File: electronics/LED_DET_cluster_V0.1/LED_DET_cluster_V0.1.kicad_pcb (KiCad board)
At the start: 2 copper layers, 15.7 x 15.7 mm, 4 parts, among them J1 Conn_01x06, J2 Conn_01x06

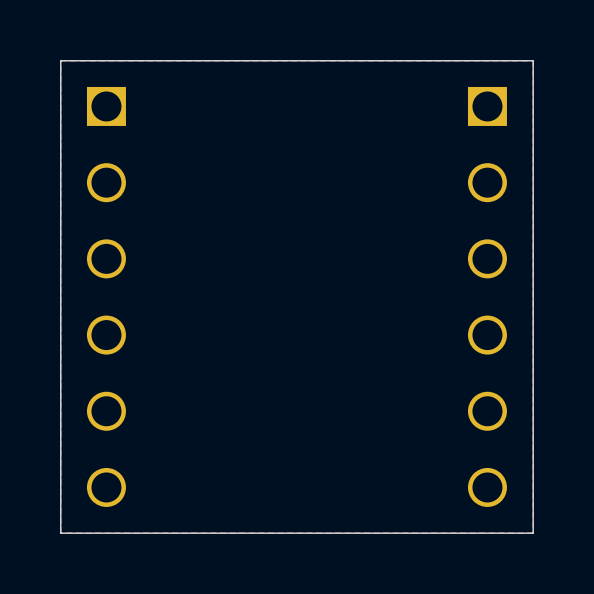
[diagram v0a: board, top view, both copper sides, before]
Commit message: completed LED detector cluster 0.1
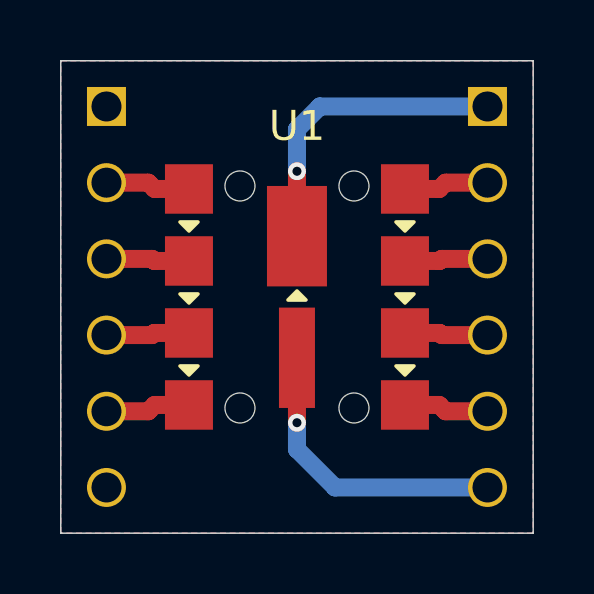
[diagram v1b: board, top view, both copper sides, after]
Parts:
- added U1: PPG_sensor_PD_4_LED, SquantorOpto:PPG_sensor_4LED, F.Cu at (139.7, 88.9)
- moved N1 2.27 mm to (139.7, 93.8)
- moved N2 1.05 mm to (139.7, 88.6)
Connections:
- J2 pad 2: /LED3A -> /LED4A
- J2 pad 3: /LED3C -> /LED4C
- J2 pad 4: /LED4A -> /LED3A
- J2 pad 5: /LED4C -> /LED3C
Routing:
- net /DET1C: track 0.00 -> 10.7 mm, vias 0 -> 1
- net /DET1A: track 0.00 -> 10.4 mm, vias 0 -> 1
- net /LED4A: track 0.00 -> 2.84 mm
- net /LED3C: track 0.00 -> 2.84 mm
- net /LED2C: track 0.00 -> 2.84 mm
- net /LED1A: track 0.00 -> 2.84 mm
- net /LED2A: track 0.00 -> 2.78 mm
- net /LED1C: track 0.00 -> 2.78 mm
- net /LED4C: track 0.00 -> 2.78 mm
- net /LED3A: track 0.00 -> 2.78 mm
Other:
- rule pad_to_mask_clearance: 0.0762 -> 0.0508
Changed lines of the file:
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@@
   )
   (setup
-    (pad_to_mask_clearance 0.0762)
-    (solder_mask_min_width 0.1016)
+    (stackup
+      (layer "F.SilkS" (type "Top Silk Screen"))
+      (layer "F.Paste" (type "Top Solder Paste"))
+      (layer "F.Mask" (type "Top Solder Mask") (thickness 0.01))
+      (layer "F.Cu" (type "copper") (thickness 0.035))
+      (layer "dielectric 1" (type "core") (thickness 1.51) (material "FR4") (epsilon_r 4.5) (loss_tangent 0.02))
+      (layer "B.Cu" (type "copper") (thickness 0.035))
+      (layer "B.Mask" (type "Bottom Solder Mask") (thickness 0.01))
+      (layer "B.Paste" (type "Bottom Solder Paste"))
+      (layer "B.SilkS" (type "Bottom Silk Screen"))
+      (copper_finish "None")
+      (dielectric_constraints no)
+    )
+    (pad_to_mask_clearance 0.0508)
     (pad_to_paste_clearance_ratio -0.1)
     (pcbplotparams
@@
   (net 10 "/LED4C")
   (net 11 "/DET1A")
+  (footprint "SquantorOpto:PPG_sensor_4LED" (layer "F.Cu")
+    (at 139.7 88.9)
+    (property "Sheetfile" "LED_DET_cluster_V0.1.kicad_sch")
+    (property "Sheetname" "")
+    (attr smd)
+    (fp_text reference "U1" (at 0 -5.7 unlocked) (layer "F.SilkS")
+      (effects (font (size 1 1) (thickness 0.15)))
+    )
+    (fp_text value "PPG_sensor_PD_4_LED" (at 0 5.7 unlocked) (layer "F.Fab")
+      (effects (font (size 1 1) (thickness 0.15)))
+    )
+    (fp_poly (pts
+        (xy -3.9 -2.5)
+        (xy -3.3 -2.5)
+        (xy -3.6 -2.2)
+      ) (layer "F.SilkS") (width 0.12) (fill solid))
+    (fp_poly (pts
+        (xy -3.9 -0.1)
+        (xy -3.3 -0.1)
+        (xy -3.6 0.2)
+      ) (layer "F.SilkS") (width 0.12) (fill solid))
+    (fp_poly (pts
+        (xy 3.3 -0.1)
+        (xy 3.9 -0.1)
+        (xy 3.6 0.2)
+      ) (layer "F.SilkS") (width 0.12) (fill solid))
+    (fp_poly (pts
+        (xy 0.3 0.1)
+        (xy -0.3 0.1)
+        (xy 0 -0.2)
+      ) (layer "F.SilkS") (width 0.12) (fill solid))
+    (fp_poly (pts
+        (xy -3.9 2.3)
+        (xy -3.3 2.3)
+        (xy -3.6 2.6)
+      ) (layer "F.SilkS") (width 0.12) (fill solid))
+    (fp_poly (pts
+        (xy 3.3 2.3)
+        (xy 3.9 2.3)
+        (xy 3.6 2.6)
+      ) (layer "F.SilkS") (width 0.12) (fill solid))
+    (fp_poly (pts
+        (xy 3.3 -2.5)
+        (xy 3.9 -2.5)
+        (xy 3.6 -2.2)
+      ) (layer "F.SilkS") (width 0.12) (fill solid))
+    (fp_rect (start -2.2 -1.95) (end 2.2 1.95) (layer "Dwgs.User") (width 0.12) (fill none))
+    (fp_line (start -4.9 5) (end -4.9 -5) (layer "F.CrtYd") (width 0.05))
+    (fp_line (start 4.9 5) (end -4.9 5) (layer "F.CrtYd") (width 0.05))
+    (fp_line (start -4.9 -5) (end 4.9 -5) (layer "F.CrtYd") (width 0.05))
+    (fp_line (start 4.9 -5) (end 4.9 5) (layer "F.CrtYd") (width 0.05))
+    (pad "" np_thru_hole circle (at 1.9 -3.7) (size 1 1) (drill 1) (layers F&B.Cu *.Mask))
+    (pad "" np_thru_hole circle (at 1.9 3.7) (size 1 1) (drill 1) (layers F&B.Cu *.Mask))
+    (pad "" np_thru_hole circle (at -1.9 3.7) (size 1 1) (drill 1) (layers F&B.Cu *.Mask))
+    (pad "" np_thru_hole circle (at -1.9 -3.7) (size 1 1) (drill 1) (layers F&B.Cu *.Mask))
+    (pad "1" smd rect (at -3.6 -3.6) (size 1.6 1.65) (layers "F.Cu" "F.Paste" "F.Mask")
+      (net 2 "/LED1A") (pintype "passive"))
+    (pad "2" smd rect (at -3.6 -1.2) (size 1.6 1.65) (layers "F.Cu" "F.Paste" "F.Mask")
+      (net 3 "/LED1C") (pintype "passive"))
+    (pad "3" smd rect (at -3.6 1.2) (size 1.6 1.65) (layers "F.Cu" "F.Paste" "F.Mask")
+      (net 4 "/LED2A") (pintype "passive"))
+    (pad "4" smd rect (at -3.6 3.6) (size 1.6 1.65) (layers "F.Cu" "F.Paste" "F.Mask")
+      (net 5 "/LED2C") (pintype "passive"))
+    (pad "5" smd rect (at 0 2.025) (size 1.2 3.35) (layers "F.Cu" "F.Paste" "F.Mask")
+      (net 11 "/DET1A") (pintype "passive"))
+    (pad "6" smd rect (at 3.6 3.6) (size 1.6 1.65) (layers "F.Cu" "F.Paste" "F.Mask")
+      (net 8 "/LED3C") (pintype "passive"))
+    (pad "7" smd rect (at 3.6 1.2) (size 1.6 1.65) (layers "F.Cu" "F.Paste" "F.Mask")
+      (net 7 "/LED3A") (pintype "passive"))
+    (pad "8" smd rect (at 3.6 -1.2) (size 1.6 1.65) (layers "F.Cu" "F.Paste" "F.Mask")
+      (net 10 "/LED4C") (pintype "passive"))
+    (pad "9" smd rect (at 3.6 -3.6) (size 1.6 1.65) (layers "F.Cu" "F.Paste" "F.Mask")
+      (net 9 "/LED4A") (pintype "passive"))
+    (pad "10" smd rect (at 0 -2.025) (size 2 3.35) (layers "F.Cu" "F.Paste" "F.Mask")
+      (net 6 "/DET1C") (pintype "passive"))
+    (model "${KICAD6_3DMODEL_DIR}/LED_SMD.3dshapes/LED_0805_2012Metric.step"
+      (offset (xyz -3.6 2.4 0))
+      (scale (xyz 1 1 1))
+      (rotate (xyz 0 0 90))
+    )
+    (model "${KICAD6_3DMODEL_DIR}/LED_SMD.3dshapes/LED_0805_2012Metric.step"
+      (offset (xyz -3.6 -2.4 0))
+      (scale (xyz 1 1 1))
+      (rotate (xyz 0 0 90))
+    )
+    (model "${KICAD6_3DMODEL_DIR}/LED_SMD.3dshapes/LED_0805_2012Metric.step"
+      (offset (xyz 3.6 -2.4 0))
+      (scale (xyz 1 1 1))
+      (rotate (xyz 0 0 90))
+    )
+    (model "${KICAD6_3DMODEL_DIR}/LED_SMD.3dshapes/LED_0805_2012Metric.step"
+      (offset (xyz 3.6 2.4 0))
+      (scale (xyz 1 1 1))
+      (rotate (xyz 0 0 90))
+    )
+  )
   (footprint "SquantorLabels:Label_Generic" (layer "B.Cu")
-    (at 139.7 91.5 180)
+    (at 139.7 93.7675 180)
     (descr "Label for general purpose use")
     (tags "Label")
@@
   )
   (footprint "Symbol:OSHW-Symbol_6.7x6mm_SilkScreen" (layer "B.Cu")
-    (at 139.7 87.6 180)
+    (at 139.7 88.646 180)
     (descr "Open Source Hardware Symbol")
     (tags "Logo Symbol OSHW")
@@
       (net 6 "/DET1C") (pinfunction "Pin_1") (pintype "passive"))
     (pad "2" thru_hole circle locked (at -3.81 0 90) (size 1.3 1.3) (drill 1) (layers *.Cu *.Mask)
-      (net 7 "/LED3A") (pinfunction "Pin_2") (pintype "passive"))
+      (net 9 "/LED4A") (pinfunction "Pin_2") (pintype "passive"))
     (pad "3" thru_hole circle locked (at -1.27 0 90) (size 1.3 1.3) (drill 1) (layers *.Cu *.Mask)
-      (net 8 "/LED3C") (pinfunction "Pin_3") (pintype "passive"))
+      (net 10 "/LED4C") (pinfunction "Pin_3") (pintype "passive"))
     (pad "4" thru_hole circle locked (at 1.27 0 90) (size 1.3 1.3) (drill 1) (layers *.Cu *.Mask)
-      (net 9 "/LED4A") (pinfunction "Pin_4") (pintype "passive"))
+      (net 7 "/LED3A") (pinfunction "Pin_4") (pintype "passive"))
     (pad "5" thru_hole circle locked (at 3.81 0 90) (size 1.3 1.3) (drill 1) (layers *.Cu *.Mask)
-      (net 10 "/LED4C") (pinfunction "Pin_5") (pintype "passive"))
+      (net 8 "/LED3C") (pinfunction "Pin_5") (pintype "passive"))
     (pad "6" thru_hole circle locked (at 6.35 0 90) (size 1.3 1.3) (drill 1) (layers *.Cu *.Mask)
       (net 11 "/DET1A") (pinfunction "Pin_6") (pintype "passive"))
@@
   (gr_line (start 147.574 96.774) (end 131.826 96.774) (layer "Edge.Cuts") (width 0.05))
   (gr_line (start 131.826 96.774) (end 131.826 81.026) (layer "Edge.Cuts") (width 0.05))
+  (segment (start 133.35 85.09) (end 134.747 85.09) (width 0.6) (layer "F.Cu") (net 2))
+  (segment (start 134.747 85.09) (end 134.957 85.3) (width 0.6) (layer "F.Cu") (net 2))
+  (segment (start 134.957 85.3) (end 136.1 85.3) (width 0.6) (layer "F.Cu") (net 2))
+  (segment (start 134.874 87.63) (end 134.944 87.7) (width 0.6) (layer "F.Cu") (net 3))
+  (segment (start 133.35 87.63) (end 134.874 87.63) (width 0.6) (layer "F.Cu") (net 3))
+  (segment (start 134.944 87.7) (end 136.1 87.7) (width 0.6) (layer "F.Cu") (net 3))
+  (segment (start 134.874 90.17) (end 134.944 90.1) (width 0.6) (layer "F.Cu") (net 4))
+  (segment (start 133.35 90.17) (end 134.874 90.17) (width 0.6) (layer "F.Cu") (net 4))
+  (segment (start 134.944 90.1) (end 136.1 90.1) (width 0.6) (layer "F.Cu") (net 4))
+  (segment (start 134.957 92.5) (end 136.1 92.5) (width 0.6) (layer "F.Cu") (net 5))
+  (segment (start 133.35 92.71) (end 134.747 92.71) (width 0.6) (layer "F.Cu") (net 5))
+  (segment (start 134.747 92.71) (end 134.957 92.5) (width 0.6) (layer "F.Cu") (net 5))
+  (segment (start 139.7 84.709) (end 139.7 87.375) (width 0.6) (layer "F.Cu") (net 6))
+  (via (at 139.7 84.709) (size 0.6) (drill 0.3) (layers "F.Cu" "B.Cu") (net 6))
+  (segment (start 139.7 84.709) (end 139.7 83.312) (width 0.6) (layer "B.Cu") (net 6))
+  (segment (start 140.462 82.55) (end 146.05 82.55) (width 0.6) (layer "B.Cu") (net 6))
+  (segment (start 139.7 83.312) (end 140.462 82.55) (width 0.6) (layer "B.Cu") (net 6))
+  (segment (start 146.05 90.17) (end 144.526 90.17) (width 0.6) (layer "F.Cu") (net 7))
+  (segment (start 144.456 90.1) (end 143.3 90.1) (width 0.6) (layer "F.Cu") (net 7))
+  (segment (start 144.526 90.17) (end 144.456 90.1) (width 0.6) (layer "F.Cu") (net 7))
+  (segment (start 146.05 92.71) (end 144.653 92.71) (width 0.6) (layer "F.Cu") (net 8))
+  (segment (start 144.443 92.5) (end 143.3 92.5) (width 0.6) (layer "F.Cu") (net 8))
+  (segment (start 144.653 92.71) (end 144.443 92.5) (width 0.6) (layer "F.Cu") (net 8))
+  (segment (start 144.443 85.3) (end 143.3 85.3) (width 0.6) (layer "F.Cu") (net 9))
+  (segment (start 146.05 85.09) (end 144.653 85.09) (width 0.6) (layer "F.Cu") (net 9))
+  (segment (start 144.653 85.09) (end 144.443 85.3) (width 0.6) (layer "F.Cu") (net 9))
+  (segment (start 144.456 87.7) (end 143.3 87.7) (width 0.6) (layer "F.Cu") (net 10))
+  (segment (start 144.526 87.63) (end 144.456 87.7) (width 0.6) (layer "F.Cu") (net 10))
+  (segment (start 146.05 87.63) (end 144.526 87.63) (width 0.6) (layer "F.Cu") (net 10))
+  (segment (start 139.7 90.425) (end 139.7 93.091) (width 0.6) (layer "F.Cu") (net 11))
+  (via (at 139.7 93.091) (size 0.6) (drill 0.3) (layers "F.Cu" "B.Cu") (net 11))
+  (segment (start 139.7 93.98) (end 140.97 95.25) (width 0.6) (layer "B.Cu") (net 11))
+  (segment (start 140.97 95.25) (end 146.05 95.25) (width 0.6) (layer "B.Cu") (net 11))
+  (segment (start 139.7 93.091) (end 139.7 93.98) (width 0.6) (layer "B.Cu") (net 11))
   (zone (net 1) (net_name "GND") (layers F&B.Cu) (hatch edge 0.508)
     (connect_pads (clearance 0.3))
